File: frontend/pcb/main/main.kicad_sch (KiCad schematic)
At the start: 31 parts, among them J1 Ext, J2 Conn_01x03, J3 Conn_01x09, J4 Debug, J5 RS485, J6 Conn_01x04, J7 Conn_01x02, Q1 MMBT3904, Q2 MMBT3904, U1 ESP32-WROOM-32, U2 AP1117-33, U3 MAX485E

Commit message: Add R10.
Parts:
- added R10: 10k, Resistor_SMD:R_0603_1608Metric, symbol Device:R
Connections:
- net B4: now also R10.2; no longer J7.2 (Pin_2), R9.2
- new net: J7.2 (Pin_2), R10.1, R9.2

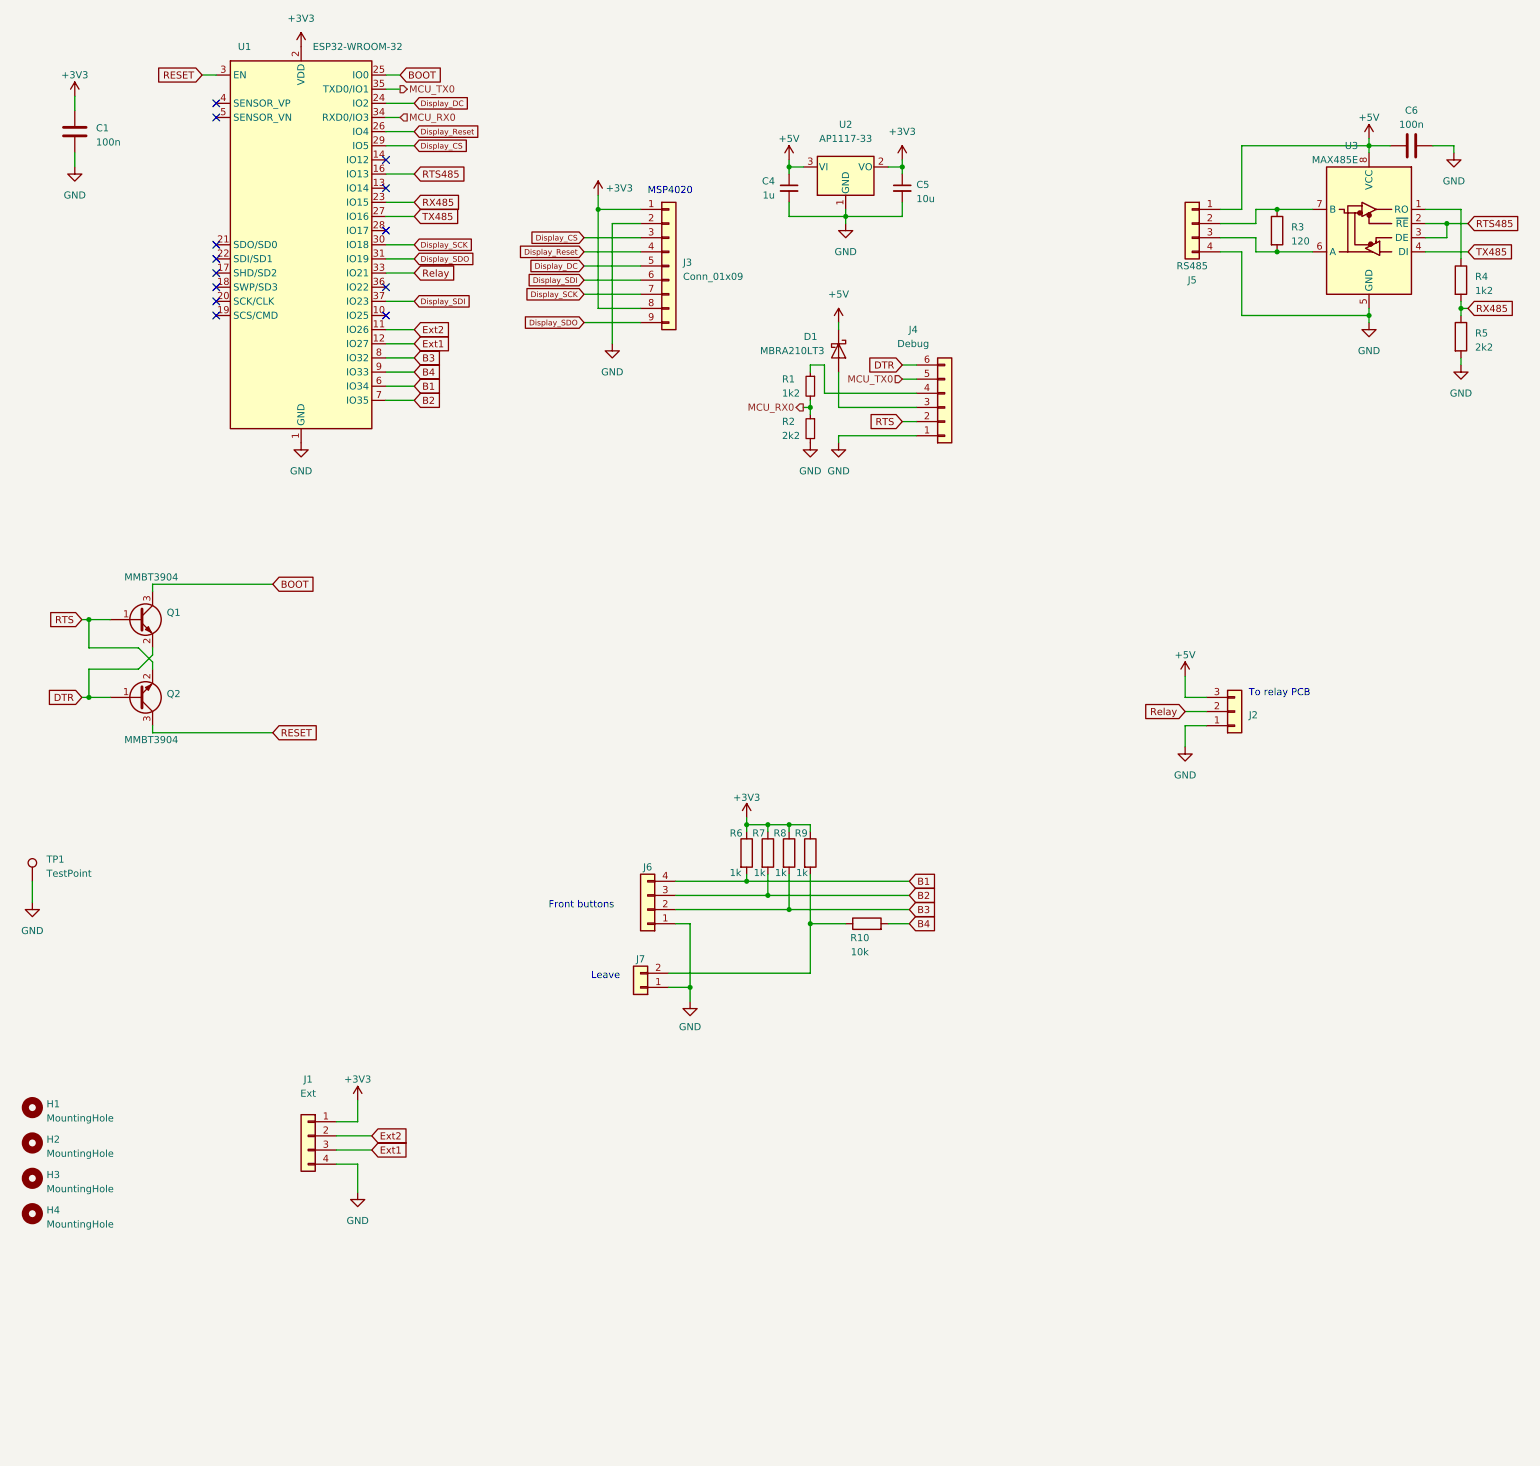
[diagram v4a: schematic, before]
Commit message: Integrate relay board components into main board. Add switches and LEDs.
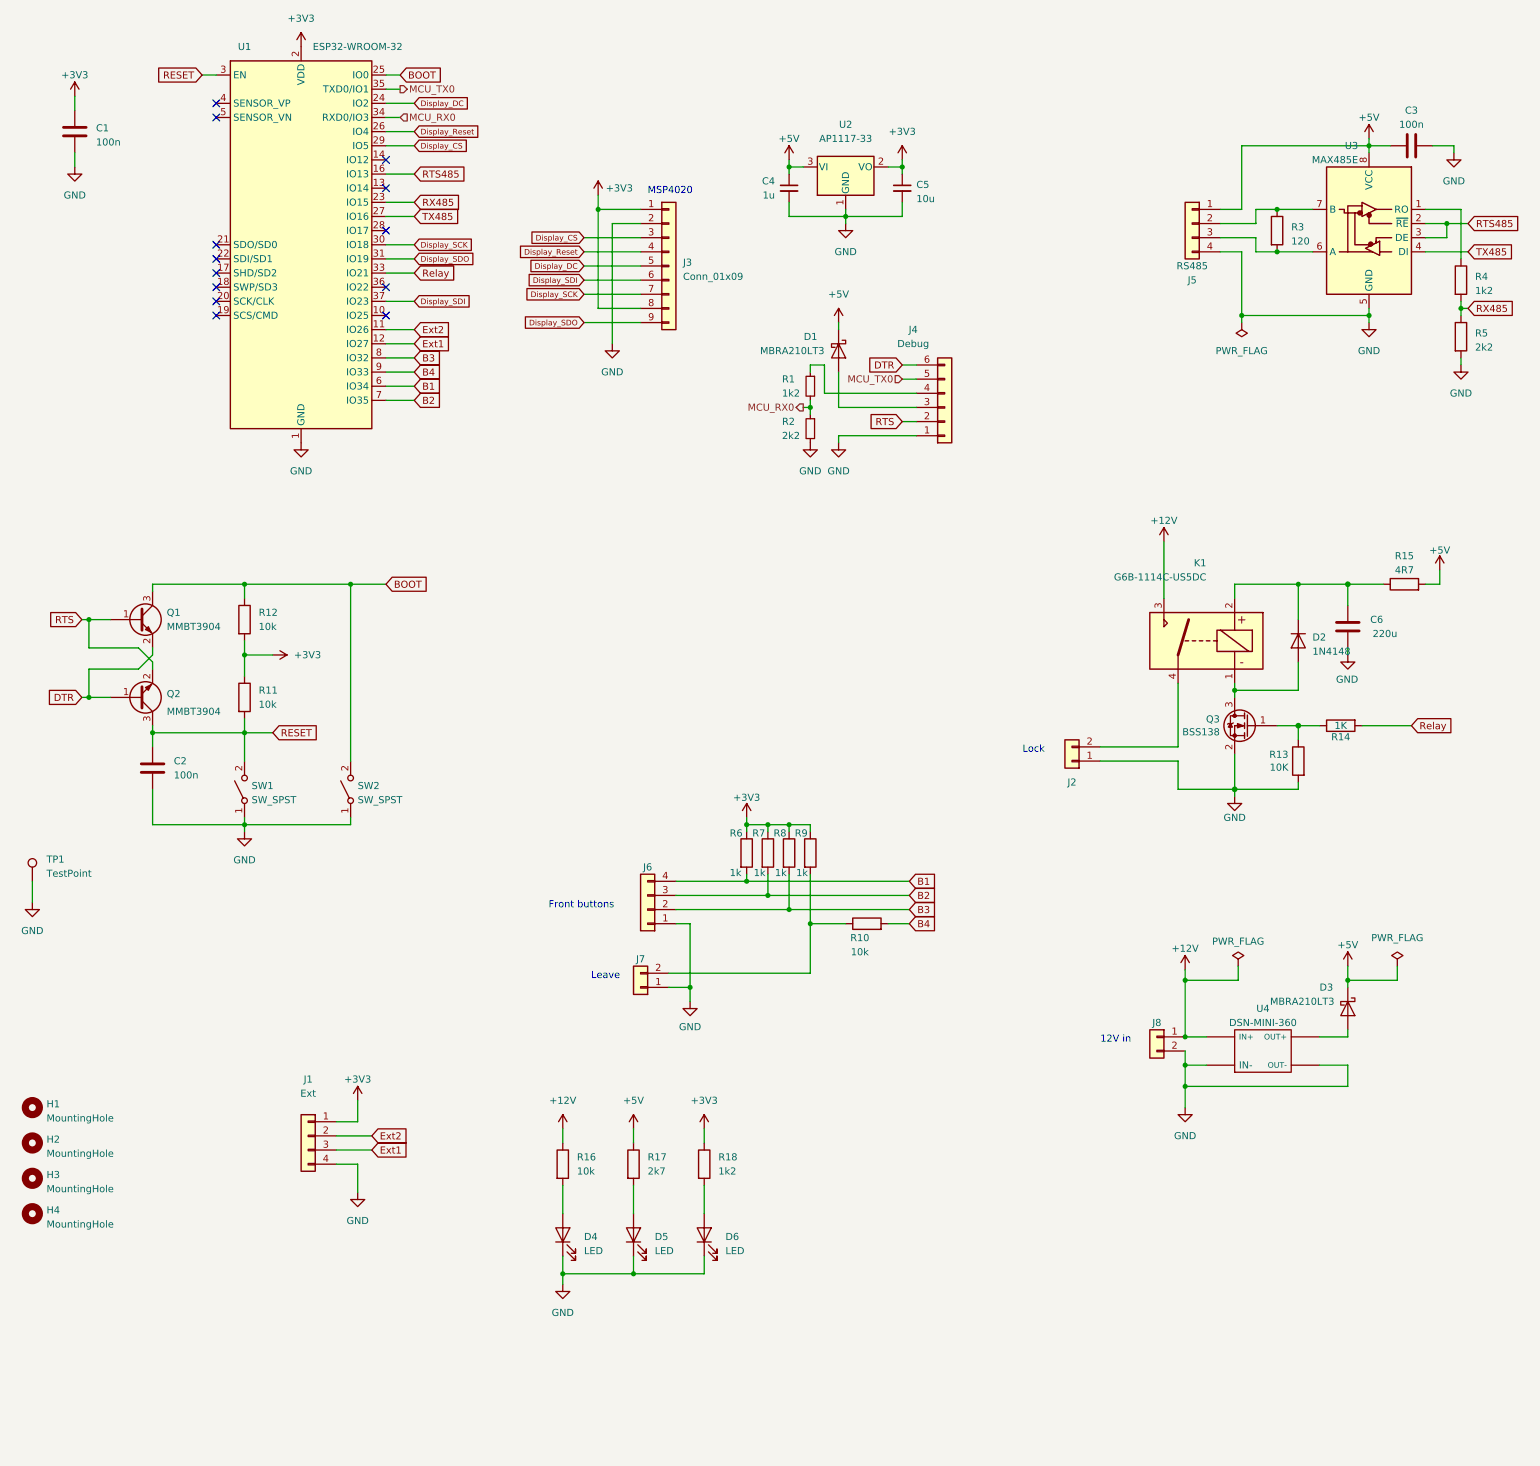
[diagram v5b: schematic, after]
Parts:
- removed J2: Conn_01x03, Connector_PinHeader_2.54mm:PinHeader_1x03_P2.54mm_Vertical, symbol Connector_Generic:Conn_01x03
- added C2: 100n, Capacitor_SMD:C_0603_1608Metric, symbol Device:C
- added C6: 220u, Capacitor_Tantalum_SMD:CP_EIA-6032-28_Kemet-C, symbol Device:C
- added D2: 1N4148, Diode_SMD:D_MiniMELF, symbol Device:D
- added D3: MBRA210LT3, Diode_SMD:D_SMA, symbol Device:D_Schottky
- added D4, D5, D6: LED, LED_SMD:LED_0603_1608Metric, symbol Device:LED
- added J2: CONN_01X02, Connector_JST:JST_XH_B2B-XH-A_1x02_P2.50mm_Vertical, symbol Connector_Generic:Conn_01x02
- added J8: Conn_01x02, Connector_JST:JST_XH_B2B-XH-A_1x02_P2.50mm_Vertical, symbol Connector_Generic:Conn_01x02
- added K1: G6B-1114C-US5DC, modules:DIL-relay, symbol g6b-1114c-us-dc5:G6B-1114C-US-DC5
- added Q3: BSS138, Package_TO_SOT_SMD:SOT-23, symbol Device:Q_NMOS_GSD
- added R11, R12, R16: 10k, Resistor_SMD:R_0603_1608Metric, symbol Device:R
- added R13: 10K, Resistor_SMD:R_0603_1608Metric, symbol Device:R
- added R14: 1K, Resistor_SMD:R_0603_1608Metric, symbol Device:R
- added R15: 4R7, Resistor_SMD:R_0603_1608Metric, symbol Device:R
- added R17: 2k7, Resistor_SMD:R_0603_1608Metric, symbol Device:R
- added R18: 1k2, Resistor_SMD:R_0603_1608Metric, symbol Device:R
- added SW1, SW2: SW_SPST, Button_Switch_SMD:SW_SPST_CK_RS282G05A3, symbol Switch:SW_SPST
- added U4: DSN-MINI-360, modules:DSN-MINI-360, symbol dsnmini360:DSN-MINI-360
- renumbered C6 to C3
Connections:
- net +3V3: now also R11.1, R12.2, R18.1
- net +5V: now also D3.1 (K), R15.2, R17.1
- net BOOT: now also R12.1, SW2.2 (B)
- net GND: now also C2.2, C6.2, D4.1 (K), D5.1 (K), D6.1 (K), J2.1 (Pin_1), J8.2 (Pin_2), Q3.2 (S), R13.2, SW1.1 (A), SW2.1 (A), U4.IN-, U4.OUT-
- net RESET: now also C2.1, R11.2, SW1.2 (B)
- net Relay: now also R14.2
- new net: D2.2 (A), K1.1, Q3.3 (D)
- new net: C6.1, D2.1 (K), K1.2, R15.1
- new net: J2.2 (Pin_2), K1.4
- new net: D3.2 (A), U4.OUT+
- new net: D4.2 (A), R16.2
- new net: D5.2 (A), R17.2
- new net: D6.2 (A), R18.2
- new net: Q3.1 (G), R13.1, R14.1
- new net +12V: J8.1 (Pin_1), K1.3, R16.1, U4.IN+
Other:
- note added: "12V in"
- note added: "Lock"
- note removed: "To relay PCB"

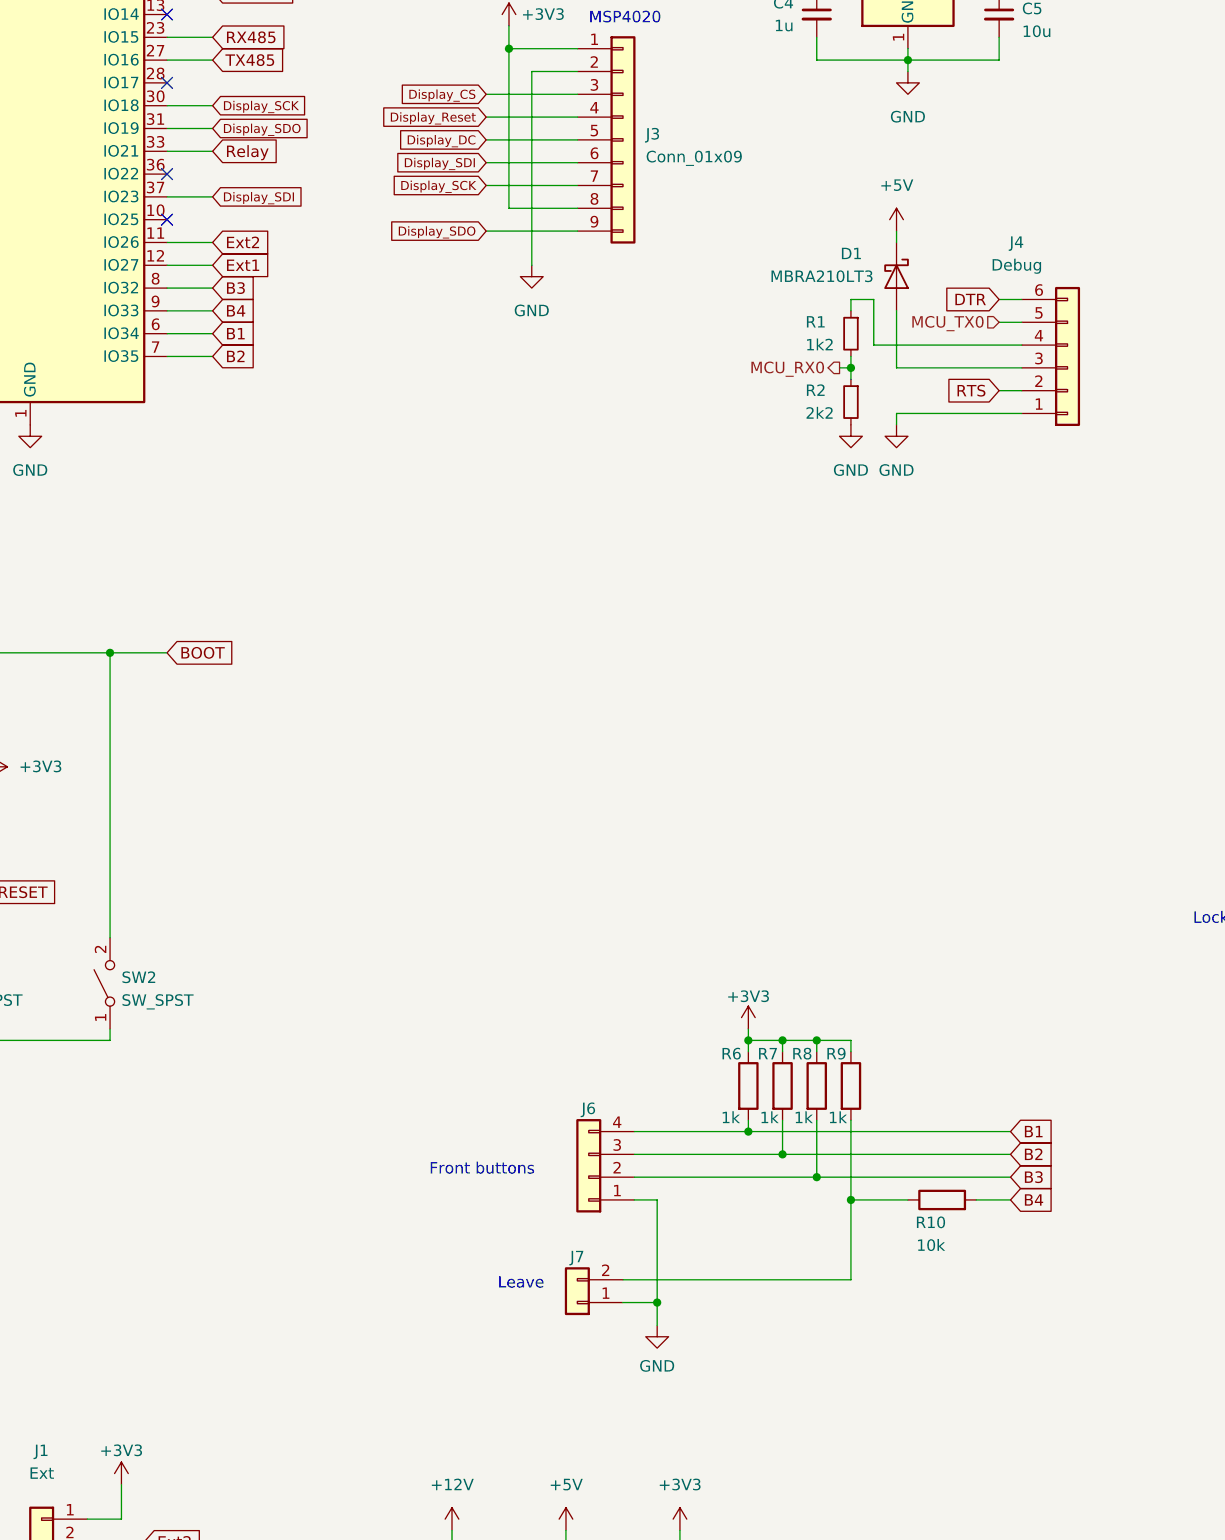
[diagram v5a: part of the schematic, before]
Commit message: Add door switch.
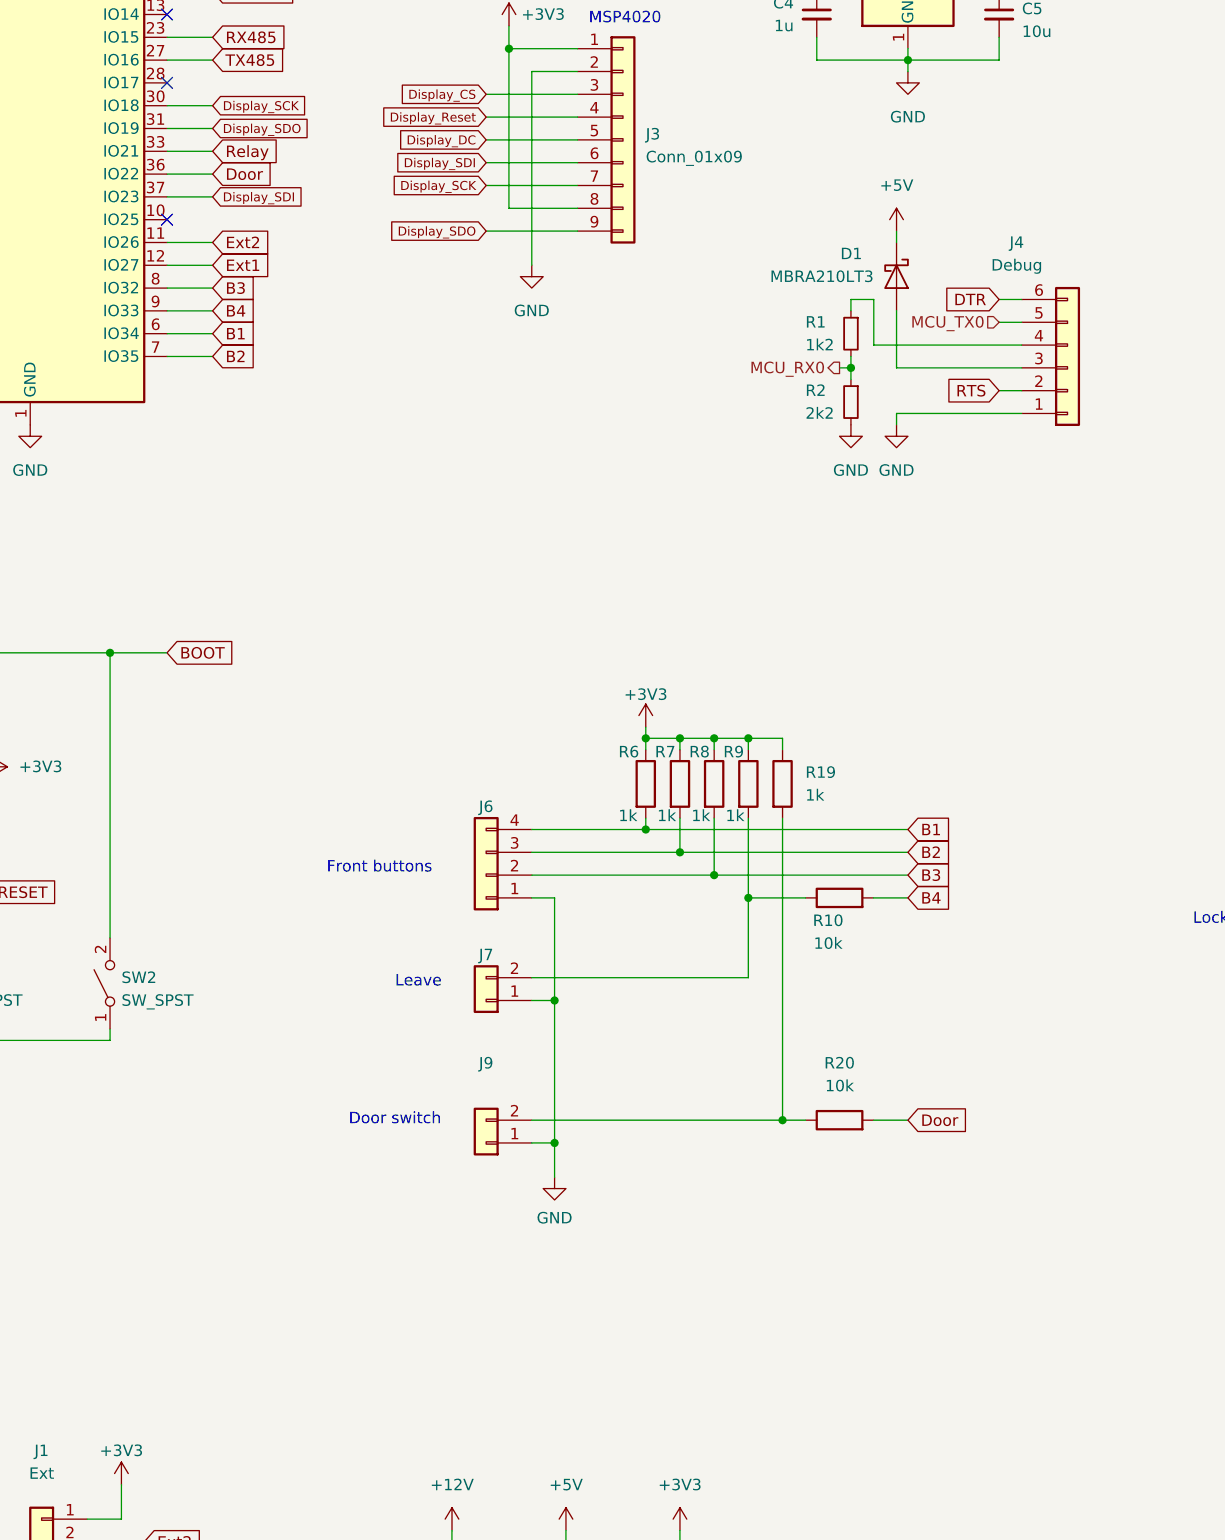
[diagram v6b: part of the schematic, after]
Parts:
- added J9: Conn_01x02, Connector_JST:JST_XH_B2B-XH-A_1x02_P2.50mm_Vertical, symbol Connector_Generic:Conn_01x02
- added R19: 1k, Resistor_SMD:R_0603_1608Metric, symbol Device:R
- added R20: 10k, Resistor_SMD:R_0603_1608Metric, symbol Device:R
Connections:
- net +3V3: now also R19.1
- net GND: now also J9.1 (Pin_1)
- net Door: now reaches U1.36 (IO22)
- net Door: now also R20.2
- new net: J9.2 (Pin_2), R19.2, R20.1
- no-connect marks 13 -> 12
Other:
- note added: "Door switch"
- moved on the sheet: J6, J7, R10, R6, R7, R8, R9
